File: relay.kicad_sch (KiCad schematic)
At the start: 11 parts, among them K27001 ALFG2PF12, Q27001 DPLS350E

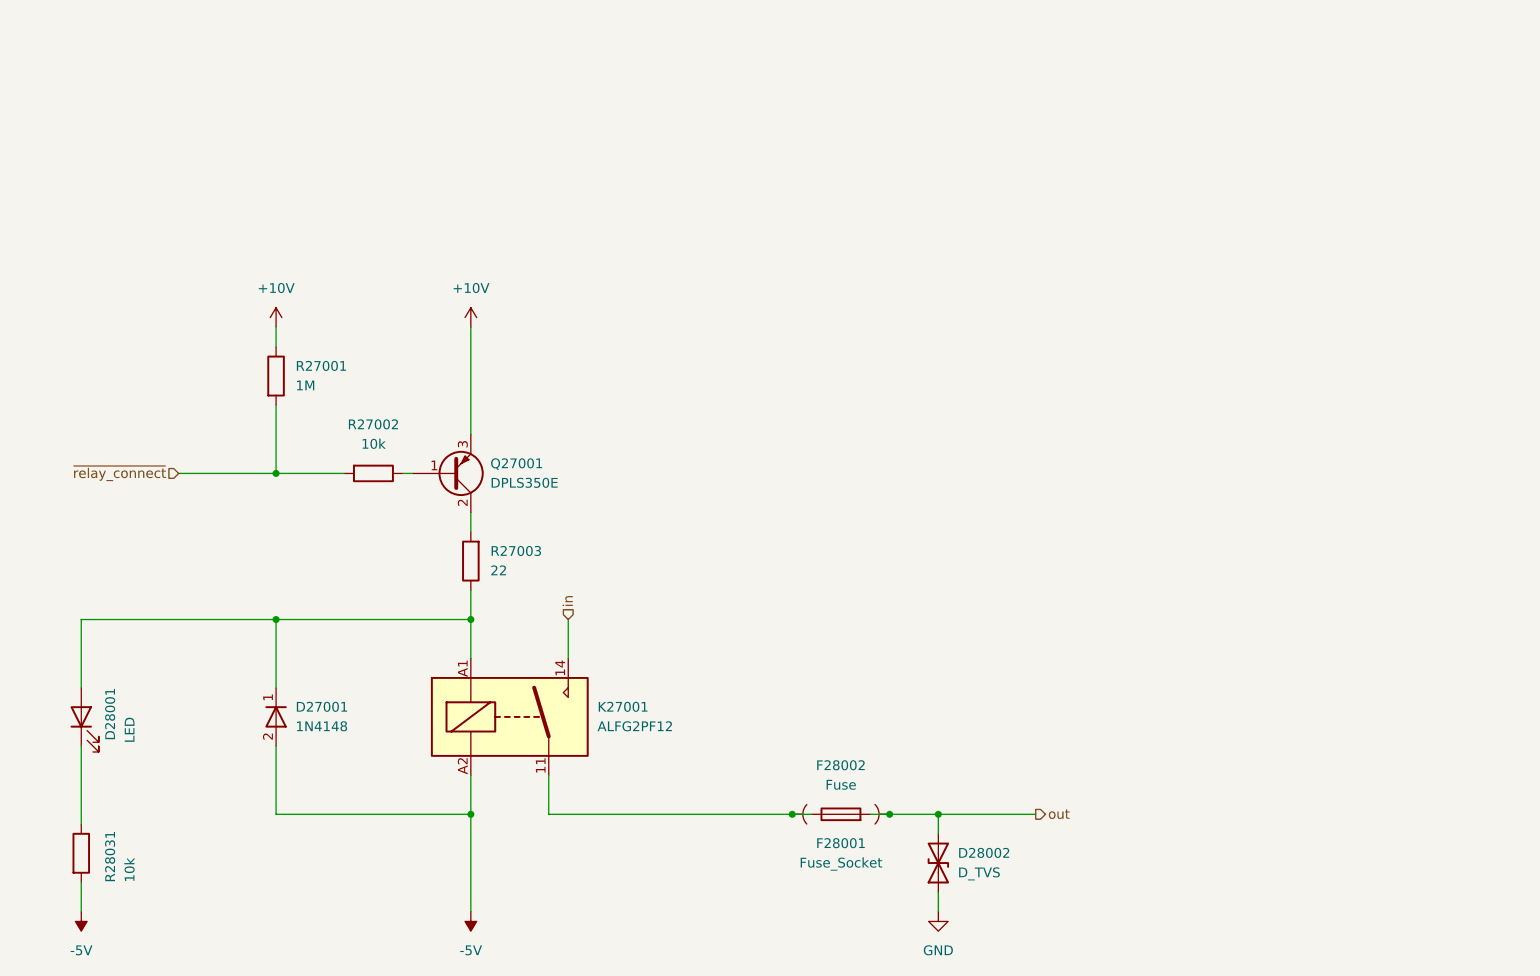
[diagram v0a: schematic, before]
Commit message: edit pss individual power nets for sub circuits
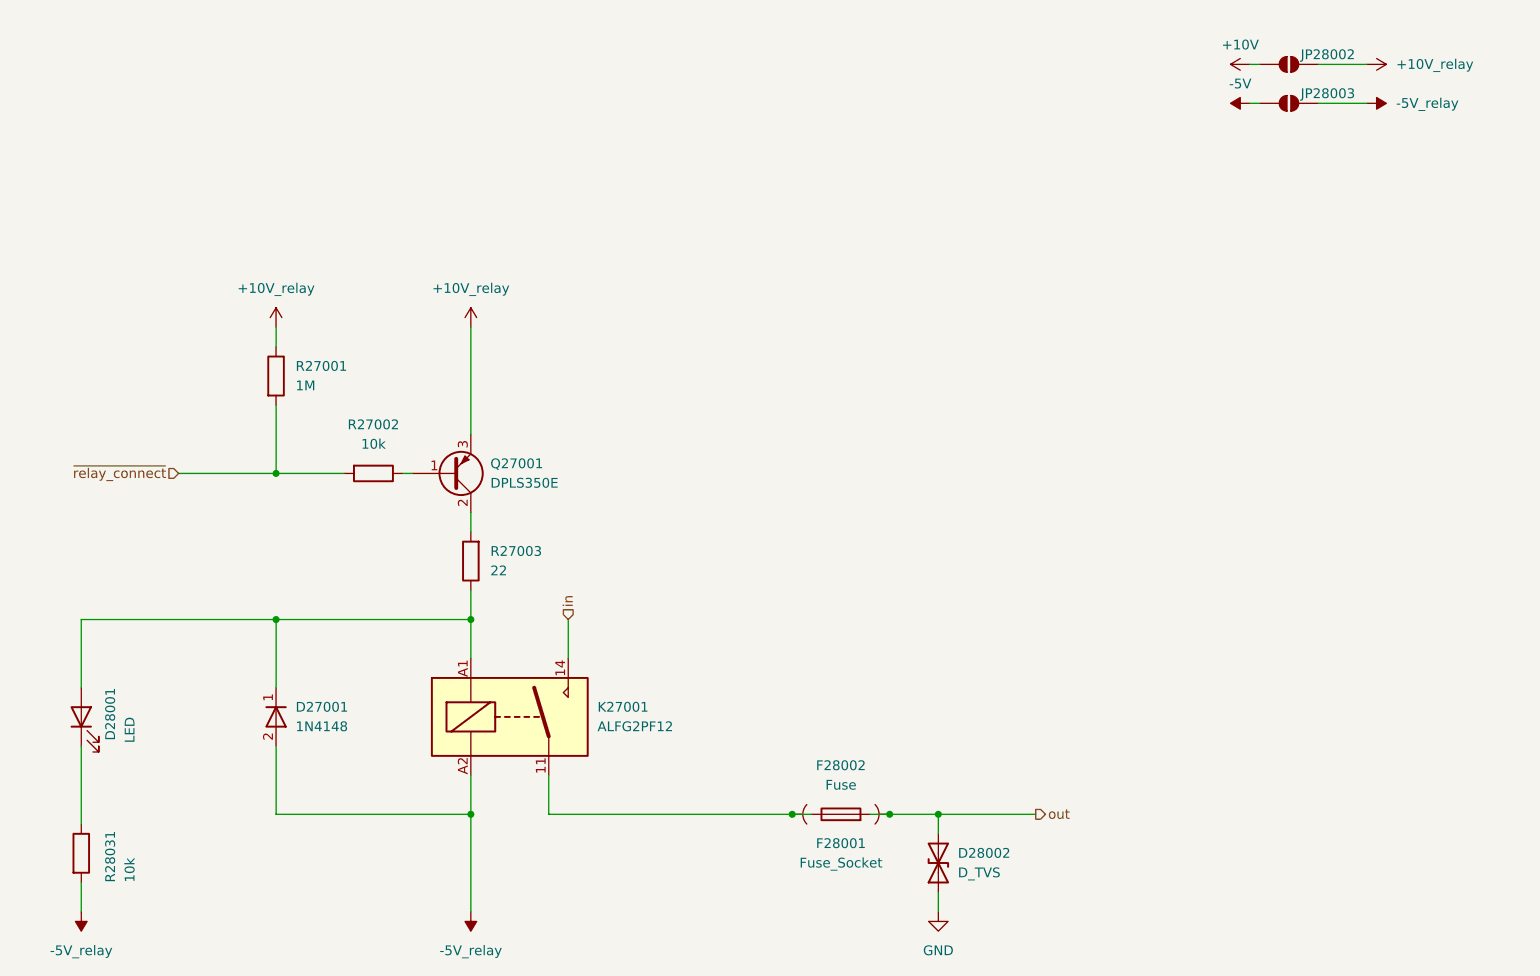
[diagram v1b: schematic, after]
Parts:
- added JP28002, JP28003: SolderJumper_2_Open, symbol Jumper:SolderJumper_2_Open
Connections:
- net +10V: now also JP28002.1 (A); no longer Q27001.3 (E), R27001.1
- net -5V: now also JP28003.1 (A); no longer D27001.2 (A), K27001.A2, R28031.2
- new net +10V_relay: JP28002.2 (B), Q27001.3 (E), R27001.1
- new net -5V_relay: D27001.2 (A), JP28003.2 (B), K27001.A2, R28031.2

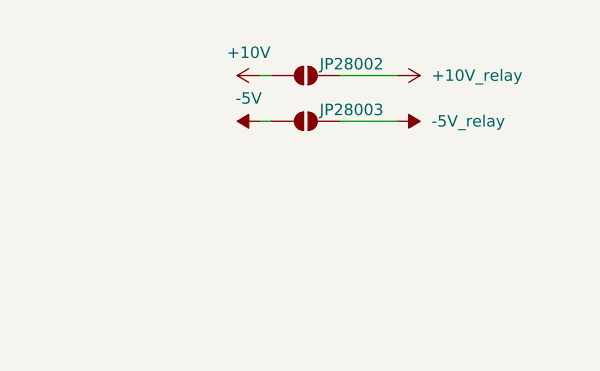
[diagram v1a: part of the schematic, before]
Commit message: fix pss ERC error: missing power flag
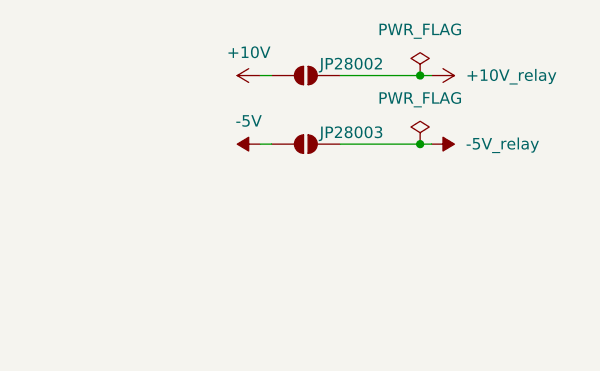
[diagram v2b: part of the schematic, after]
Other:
- moved on the sheet: JP28003
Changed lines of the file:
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@@
+	)
+	(junction
+		(at 261.62 36.83)
+		(diameter 0)
+		(color 0 0 0 0)
 	)
 	(junction
@@
 	)
 	(junction
+		(at 261.62 29.21)
+		(diameter 0)
+		(color 0 0 0 0)
+	)
+	(junction
 		(at 196.85 127)
 		(diameter 0)
@@
 	(wire
 		(pts
+			(xy 261.62 29.21) (xy 262.89 29.21)
+		)
+		(stroke
+			(width 0)
+			(type default)
+		)
+	)
+	(wire
+		(pts
 			(xy 116.84 118.11) (xy 116.84 127)
 		)
@@
 	(wire
 		(pts
-			(xy 243.84 34.29) (xy 245.11 34.29)
+			(xy 243.84 36.83) (xy 245.11 36.83)
 		)
 		(stroke
@@
 	(wire
 		(pts
-			(xy 252.73 29.21) (xy 259.08 29.21)
+			(xy 252.73 29.21) (xy 261.62 29.21)
 		)
 		(stroke
@@
 	(wire
 		(pts
+			(xy 261.62 36.83) (xy 262.89 36.83)
+		)
+		(stroke
+			(width 0)
+			(type default)
+		)
+	)
+	(wire
+		(pts
 			(xy 203.2 127) (xy 215.9 127)
 		)
@@
 	(wire
 		(pts
-			(xy 252.73 34.29) (xy 259.08 34.29)
+			(xy 252.73 36.83) (xy 261.62 36.83)
 		)
 		(stroke
@@
 	)
 	(symbol
-		(lib_id "pss:-5V_relay")
-		(at 259.08 34.29 270)
+		(lib_id "pss:PWR_FLAG")
+		(at 261.62 29.21 0)
 		(unit 1)
 		(exclude_from_sim no)
@@
 		(dnp no)
 		(fields_autoplaced yes)
+		(property "Reference" "#FLG028001"
+			(at 261.62 27.305 0)
+			(effects
+				(font
+					(size 1.27 1.27)
+				)
+				(hide yes)
+			)
+		)
+		(property "Value" "PWR_FLAG"
+			(at 261.62 24.13 0)
+			(effects
+				(font
+					(size 1.27 1.27)
+				)
+			)
+		)
+		(property "Footprint" ""
+			(at 261.62 29.21 0)
+			(effects
+				(font
+					(size 1.27 1.27)
+				)
+				(hide yes)
+			)
+		)
+		(property "Datasheet" "~"
+			(at 261.62 29.21 0)
+			(effects
+				(font
+					(size 1.27 1.27)
+				)
+				(hide yes)
+			)
+		)
+		(property "Description" "Special symbol for telling ERC where power comes from"
+			(at 261.62 29.21 0)
+			(effects
+				(font
+					(size 1.27 1.27)
+				)
+				(hide yes)
+			)
+		)
+		(pin "1"
+		)
+		(instances
+			(project "pss"
+				(path "/3c438cf7-9350-4e9f-8115-1deba8984176/20918679-4743-4169-a60e-19637ed5d643"
+					(reference "#FLG028001")
+					(unit 1)
+				)
+			)
+		)
+	)
+	(symbol
+		(lib_id "pss:-5V_relay")
+		(at 262.89 36.83 270)
+		(unit 1)
+		(exclude_from_sim no)
+		(in_bom yes)
+		(on_board yes)
+		(dnp no)
+		(fields_autoplaced yes)
 		(property "Reference" "#PWR028036"
-			(at 255.27 34.29 0)
+			(at 259.08 36.83 0)
 			(effects
 				(font
@@
 		)
 		(property "Value" "-5V_relay"
-			(at 262.89 34.2899 90)
+			(at 266.7 36.8299 90)
 			(effects
 				(font
@@
 		)
 		(property "Footprint" ""
-			(at 259.08 34.29 0)
+			(at 262.89 36.83 0)
 			(effects
 				(font
@@
 		)
 		(property "Datasheet" ""
-			(at 259.08 34.29 0)
+			(at 262.89 36.83 0)
 			(effects
 				(font
@@
 		)
 		(property "Description" ""
-			(at 259.08 34.29 0)
+			(at 262.89 36.83 0)
 			(effects
 				(font
@@
 	(symbol
 		(lib_id "Jumper:SolderJumper_2_Open")
-		(at 248.92 34.29 0)
+		(at 248.92 36.83 0)
 		(unit 1)
 		(exclude_from_sim yes)
@@
 		(dnp no)
 		(property "Reference" "JP28003"
-			(at 254 33.02 0)
+			(at 254 35.56 0)
 			(effects
 				(font
@@
 		)
 		(property "Value" "SolderJumper_2_Open"
-			(at 223.52 21.59 0)
+			(at 223.52 24.13 0)
 			(effects
 				(font
@@
 		)
 		(property "Footprint" ""
-			(at 248.92 34.29 0)
+			(at 248.92 36.83 0)
 			(effects
 				(font
@@
 		)
 		(property "Datasheet" "~"
-			(at 248.92 34.29 0)
+			(at 248.92 36.83 0)
 			(effects
 				(font
@@
 		)
 		(property "Description" "Solder Jumper, 2-pole, open"
-			(at 248.92 34.29 0)
+			(at 248.92 36.83 0)
 			(effects
 				(font
@@
 	)
 	(symbol
+		(lib_id "pss:PWR_FLAG")
+		(at 261.62 36.83 0)
+		(unit 1)
+		(exclude_from_sim no)
+		(in_bom yes)
+		(on_board yes)
+		(dnp no)
+		(fields_autoplaced yes)
+		(property "Reference" "#FLG028002"
+			(at 261.62 34.925 0)
+			(effects
+				(font
+					(size 1.27 1.27)
+				)
+				(hide yes)
+			)
+		)
+		(property "Value" "PWR_FLAG"
+			(at 261.62 31.75 0)
+			(effects
+				(font
+					(size 1.27 1.27)
+				)
+			)
+		)
+		(property "Footprint" ""
+			(at 261.62 36.83 0)
+			(effects
+				(font
+					(size 1.27 1.27)
+				)
+				(hide yes)
+			)
+		)
+		(property "Datasheet" "~"
+			(at 261.62 36.83 0)
+			(effects
+				(font
+					(size 1.27 1.27)
+				)
+				(hide yes)
+			)
+		)
+		(property "Description" "Special symbol for telling ERC where power comes from"
+			(at 261.62 36.83 0)
+			(effects
+				(font
+					(size 1.27 1.27)
+				)
+				(hide yes)
+			)
+		)
+		(pin "1"
+		)
+		(instances
+			(project "pss"
+				(path "/3c438cf7-9350-4e9f-8115-1deba8984176/20918679-4743-4169-a60e-19637ed5d643"
+					(reference "#FLG028002")
+					(unit 1)
+				)
+			)
+		)
+	)
+	(symbol
 		(lib_id "pss:Q_PNP_BCE")
 		(at 139.7 82.55 0)
@@
 	(symbol
 		(lib_id "pss:+10V_relay")
-		(at 259.08 29.21 270)
+		(at 262.89 29.21 270)
 		(unit 1)
 		(exclude_from_sim no)
@@
 		(fields_autoplaced yes)
 		(property "Reference" "#PWR028044"
-			(at 255.27 29.21 0)
+			(at 259.08 29.21 0)
 			(effects
 				(font
@@
 		)
 		(property "Value" "+10V_relay"
-			(at 262.89 29.2099 90)
+			(at 266.7 29.2099 90)
 			(effects
 				(font
@@
 		)
 		(property "Footprint" ""
-			(at 259.08 29.21 0)
+			(at 262.89 29.21 0)
 			(effects
 				(font
@@
 		)
 		(property "Datasheet" ""
-			(at 259.08 29.21 0)
+			(at 262.89 29.21 0)
 			(effects
 				(font
@@
 		)
 		(property "Description" ""
-			(at 259.08 29.21 0)
+			(at 262.89 29.21 0)
 			(effects
 				(font
@@
 	(symbol
 		(lib_id "pss:-5V")
-		(at 243.84 34.29 90)
+		(at 243.84 36.83 90)
 		(unit 1)
 		(exclude_from_sim no)
@@
 		(fields_autoplaced yes)
 		(property "Reference" "#PWR028014"
-			(at 247.65 34.29 0)
+			(at 247.65 36.83 0)
 			(effects
 				(font
@@
 		)
 		(property "Value" "-5V"
-			(at 242.57 31.75 90)
+			(at 242.57 34.29 90)
 			(effects
 				(font
@@
 		)
 		(property "Footprint" ""
-			(at 243.84 34.29 0)
+			(at 243.84 36.83 0)
 			(effects
 				(font
@@
 		)
 		(property "Datasheet" ""
-			(at 243.84 34.29 0)
+			(at 243.84 36.83 0)
 			(effects
 				(font
@@
 		)
 		(property "Description" "Power symbol creates a global label with name \"-5V\""
-			(at 243.84 34.29 0)
-			(effects
-				(font
+			(at 243.84 36.83 0)
+			(effects
+				(font

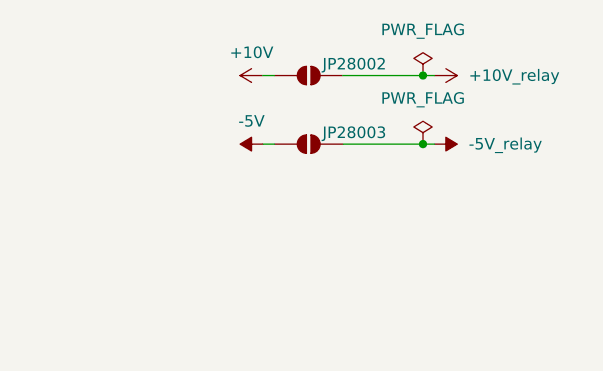
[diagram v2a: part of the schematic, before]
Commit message: fix pss ERC errors: multiple outputs connected
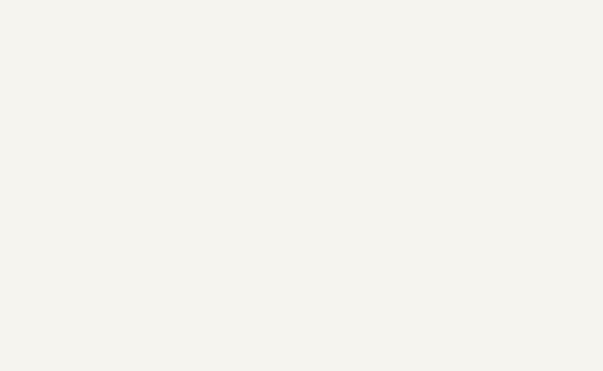
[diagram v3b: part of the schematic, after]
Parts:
- removed JP28002, JP28003: SolderJumper_2_Open, symbol Jumper:SolderJumper_2_Open
